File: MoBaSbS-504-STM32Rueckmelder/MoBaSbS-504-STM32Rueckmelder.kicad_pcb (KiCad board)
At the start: 2 copper layers, 46.2 x 69.6 mm, 15 parts, among them IC1 TJA1057BT, J1 RJ45, J2 RJ45, J3 Conn_02x05_Counter_Clockwise, J4 Conn_01x03, J5 Conn_02x05_Counter_Clockwise, J6 Conn_01x03, P1 PSS254

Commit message: Only some finishing touches left
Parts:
- added J7: Conn_02x03_Odd_Even, Connector_PinHeader_2.54mm:PinHeader_2x03_P2.54mm_Horizontal, F.Cu at (90.1, 128.3)
- moved H4 10.7 mm to (97.2, 128.3)
- moved P1 2.29 mm to (96.0, 123.2)
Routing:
- net Net-(IC1-CANL): track 29.8 -> 44.3 mm
- net +5V: track 118.3 -> 131.8 mm
- net Net-(IC1-CANH): track 28.1 -> 34.2 mm
- net GND: vias 23 -> 25

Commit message: Some more work
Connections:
- J1 pad 4: unconnected-(J1-Pin_4-Pad4) -> Net-(J1-Pin_4)
- J1 pad 5: unconnected-(J1-Pin_5-Pad5) -> Net-(J1-Pin_5)
- J2 pad 4: unconnected-(J2-Pin_4-Pad4) -> Net-(J1-Pin_4)
- J2 pad 5: unconnected-(J2-Pin_5-Pad5) -> Net-(J1-Pin_5)
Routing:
- net Net-(J1-Pin_4): track 0.00 -> 23.8 mm
- net Net-(J1-Pin_5): track 0.00 -> 21.1 mm
- net Net-(IC1-CANH): track 34.2 -> 33.7 mm
- net Net-(IC1-CANL): track 44.3 -> 43.8 mm

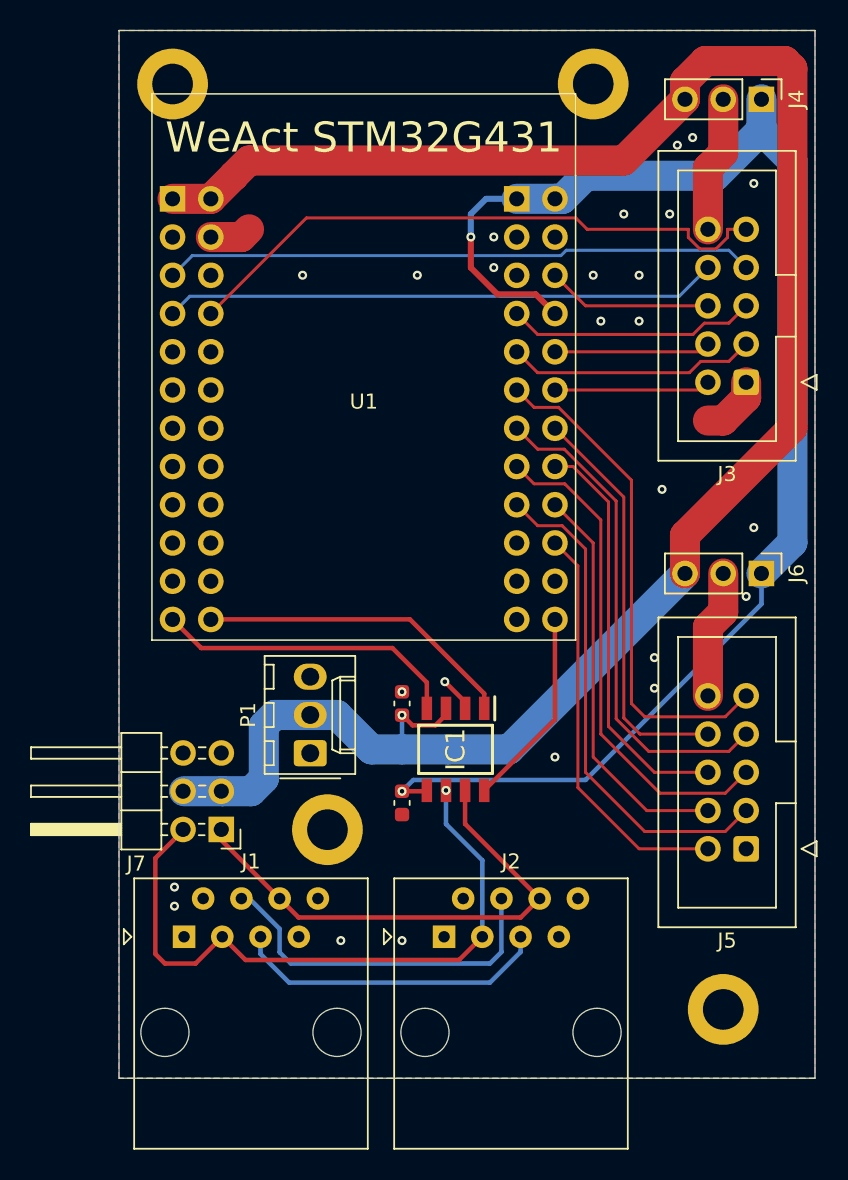
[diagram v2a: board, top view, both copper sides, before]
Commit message: Generated panels, added some new PCBs
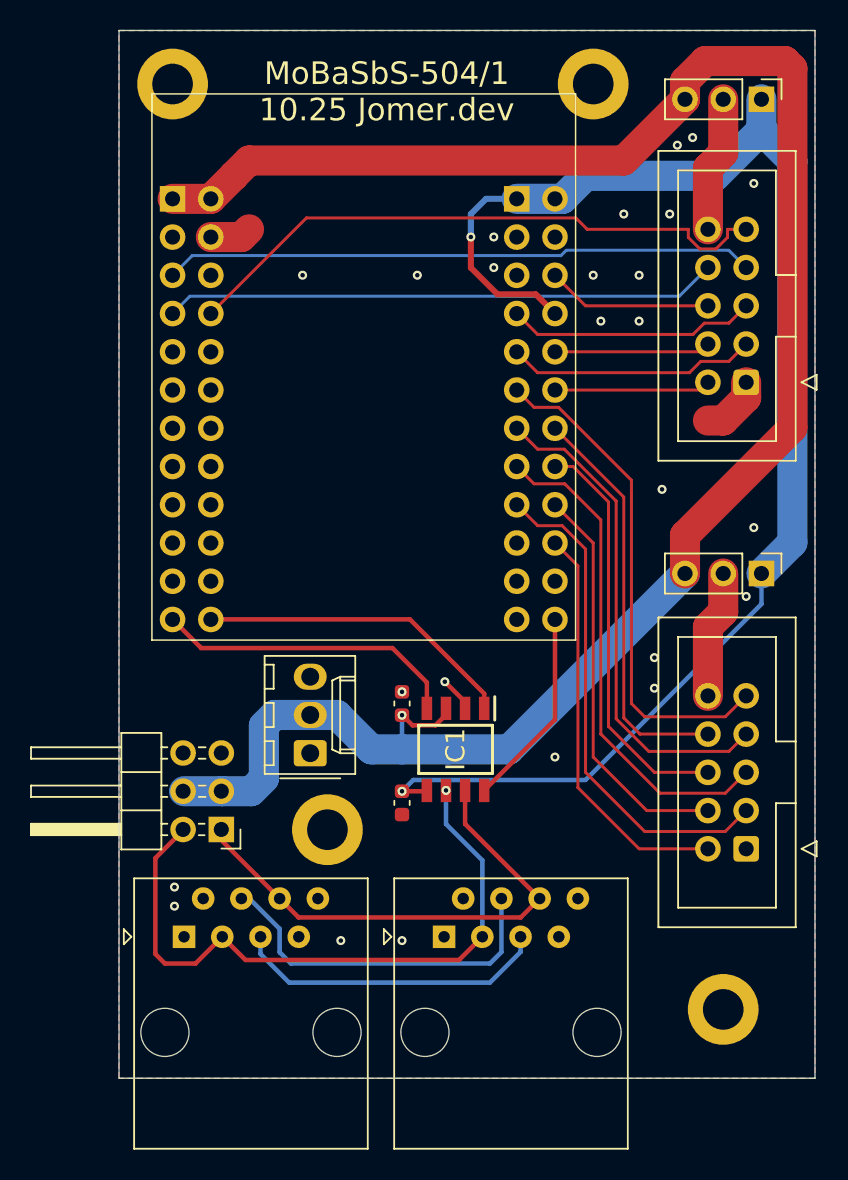
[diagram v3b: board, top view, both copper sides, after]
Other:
- board text added: "MoBaSbS-504/1 10.25 Jomer.dev"
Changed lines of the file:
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@@
 			(psa4output no)
 			(plot_black_and_white yes)
-			(plotinvisibletext no)
 			(sketchpadsonfab no)
 			(plotpadnumbers no)
@@
 			(at 0 -2.33 90)
 			(layer "F.SilkS")
+			(hide yes)
 			(effects
 				(font
@@
 			(at 1.27 -6.1 0)
 			(layer "F.SilkS")
+			(hide yes)
 			(effects
 				(font
@@
 			(at 2.54 -4.12 90)
 			(layer "F.SilkS")
+			(hide yes)
 			(effects
 				(font
@@
 			(unlocked yes)
 			(layer "F.SilkS")
+			(hide yes)
 			(effects
 				(font
@@
 			(layer "F.SilkS")
 		)
-		(fp_text user "WeAct STM32G431"
-			(at 0 -18.034 0)
-			(unlocked yes)
-			(layer "F.SilkS")
-			(effects
-				(font
-					(size 2 2)
-					(thickness 0.1)
-				)
-			)
-		)
 		(fp_text user "${REFERENCE}"
 			(at 0 2.5 0)
@@
 			(at 4.445 -5 0)
 			(layer "F.SilkS")
+			(hide yes)
 			(effects
 				(font
@@
 			(at 4.445 4 0)
 			(layer "F.Fab")
+			(hide yes)
 			(effects
 				(font
@@
 			(at 0 -2.33 90)
 			(layer "F.SilkS")
+			(hide yes)
 			(effects
 				(font
@@
 			(at 5.655 -2.27 0)
 			(layer "F.SilkS")
+			(hide yes)
 			(effects
 				(font
@@
 			(at 1.27 -6.1 0)
 			(layer "F.SilkS")
+			(hide yes)
 			(effects
 				(font
@@
 			(at 4.445 -5 0)
 			(layer "F.SilkS")
+			(hide yes)
 			(effects
 				(font
@@
 			(at 4.445 4 0)
 			(layer "F.Fab")
+			(hide yes)
 			(effects
 				(font
@@
 		(layer "Edge.Cuts")
 	)
+	(gr_text "MoBaSbS-504/1\n10.25 Jomer.dev"
+		(at 101.092 79.248 0)
+		(layer "F.SilkS")
+		(effects
+			(font
+				(size 1.5 1.5)
+				(thickness 0.3)
+			)
+		)
+	)
 	(segment
